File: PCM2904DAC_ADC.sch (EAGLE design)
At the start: 27 parts, among them Q1 12MHz, X1 V+, D-, D+, GND, X2 1503_09, X3 1503_09

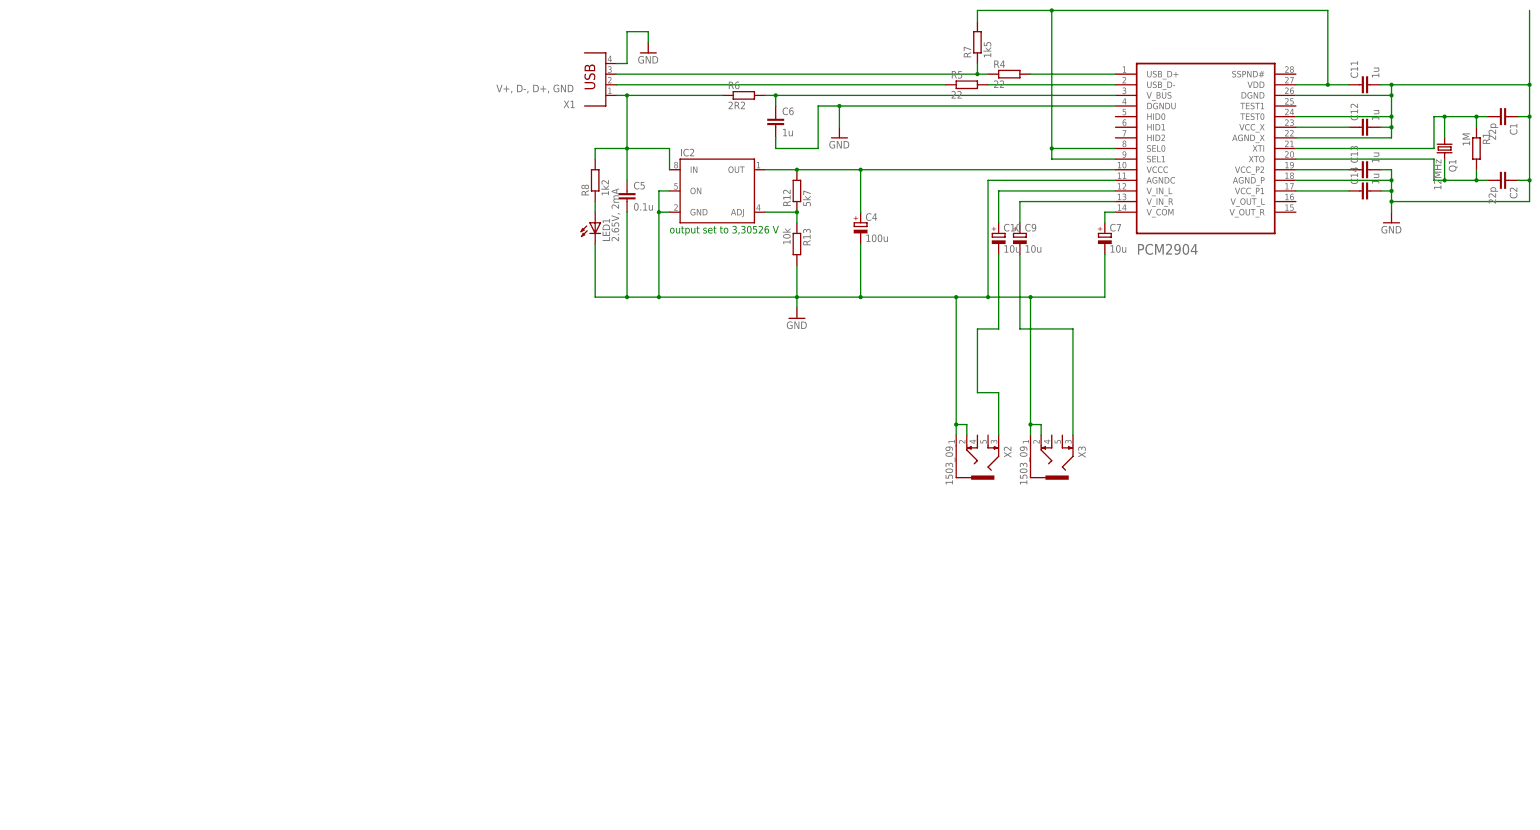
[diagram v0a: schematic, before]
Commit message: Agregados etapas preamplificadoras...
... y cambiado el ordenamiento y routeo de pistas
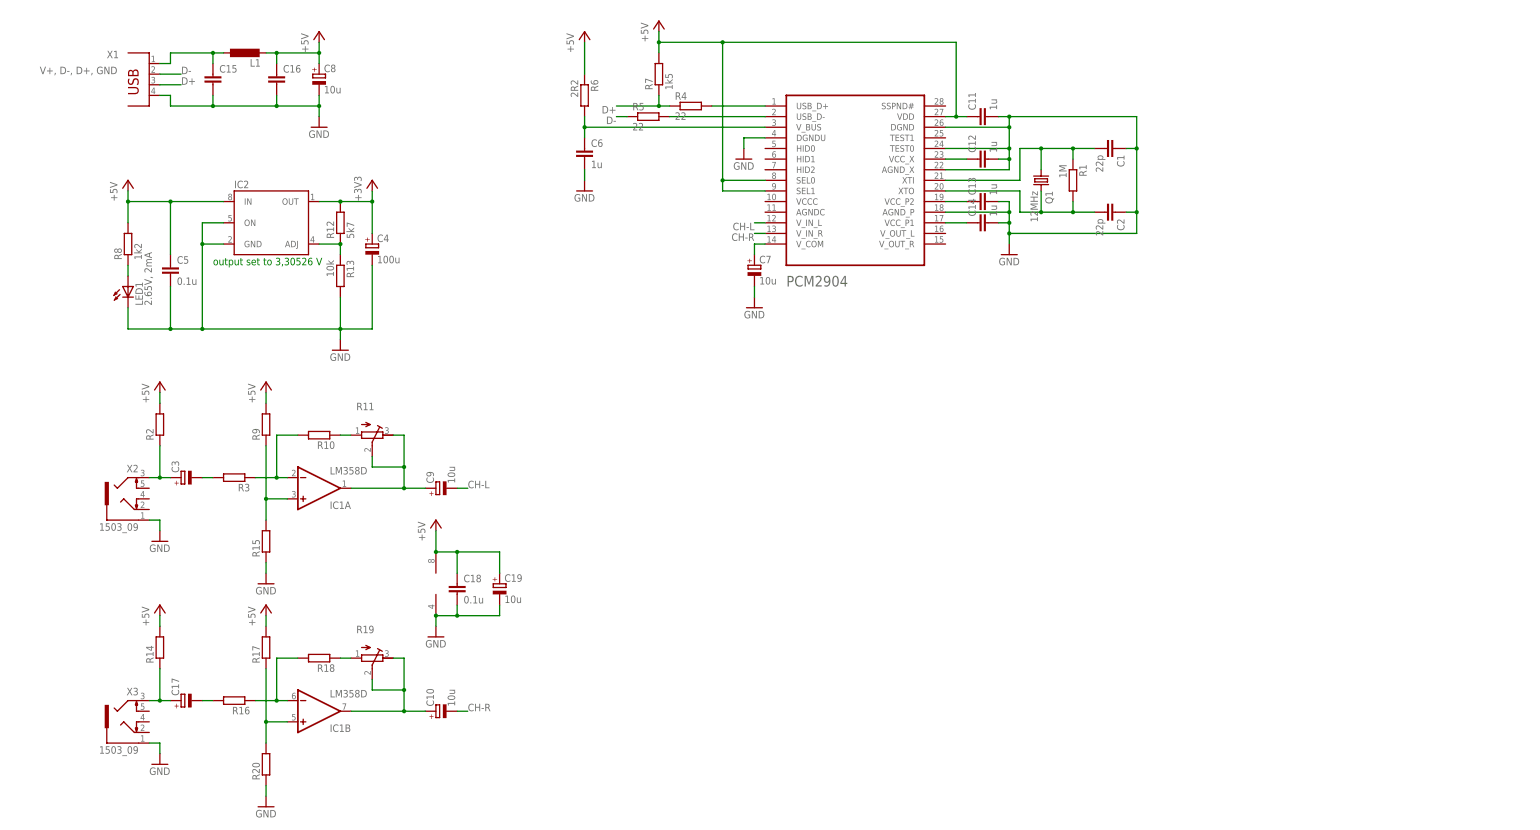
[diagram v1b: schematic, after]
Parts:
- added C15, C16: (no value), rcl:C-EUC1206K
- added C17, C3: (no value), rcl:CPOL-EU153CLV-0810
- added C18: 0.1u, rcl:C-EUC1206
- added C19, C8: 10u, rcl:CPOL-EUE2-4
- added IC1: LM358D, linear:LM358D
- added L1: (no value), rcl:L-EU0207/7
- added R10, R14, R15, R16, R17, R18, R2, R20, R3, R9: (no value), rcl:R-EU_R1206W
- added R11, R19: (no value), rcl:R-TRIMM64W
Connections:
- net N$7 renamed D+
- net N$8 renamed D-
- removed net N$40: C4.+, IC2.OUT, PCM2904.VCCC, R12.2
- new net +3V3: C4.+, IC2.OUT, R12.2
- new net +5V: C11.1, C16.1, C18.1, C19.+, C5.1, C8.+, IC1P.V+, IC2.IN, L1.2, PCM2904.SEL0, PCM2904.SEL1, PCM2904.VDD, R14.2, R17.2, R2.2, R6.1, R7.2, R8.2, R9.2
- new net CH-L: C9.-, PCM2904.V_IN_L
- new net CH-R: C10.-, PCM2904.V_IN_R
- new net N$17: R10.1, R11.A
- new net N$18: C9.+, IC1A.OUT, R11.E, R11.S
- new net N$19: IC1A.+IN, R15.2, R9.1
- new net N$22: IC1B.+IN, R17.1, R20.2
- new net N$5: C3.+, R2.1, X2.3
- new net N$7: C17.+, R14.1, X3.3
- new net N$8: C15.1, L1.1, X1.1
- net GND: now also C15.2, C16.2, C18.2, C19.-, C8.-, IC1P.V-, R15.1, R20.1; no longer PCM2904.AGNDC, X2.2, X3.2
- net N$10: now also IC1B.-IN, R16.1, R18.2; no longer C10.+, PCM2904.V_IN_L
- net N$12: now also R18.1, R19.A; no longer C11.1, PCM2904.SEL0, PCM2904.SEL1, PCM2904.VDD, R7.2
- net N$13: now also C3.-, R3.2; no longer C10.-, X2.3
- net N$14: now also C10.+, IC1B.OUT, R19.E, R19.S; no longer C9.+, PCM2904.V_IN_R
- net N$15: now also IC1A.-IN, R10.2, R3.1; no longer C9.-, X3.3
- net N$9: now also C17.-, R16.2; no longer C5.1, IC2.IN, R6.1, R8.2, X1.1
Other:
- moved on the sheet: C1, C10, C11, C12, C13, C14, C2, C4, C5, C6, C7, C9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

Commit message: Commit adicional
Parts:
- C10, C19, C8, C9: device rcl:CPOL-EUE2-4 -> rcl:CPOL-EU153CLV-0505
- C17, C3: device rcl:CPOL-EU153CLV-0810 -> rcl:CPOL-EU153CLV-0505
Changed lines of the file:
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@@
 <part name="GND4" library="supply1" deviceset="GND" device=""/>
 <part name="C7" library="rcl" deviceset="CPOL-EU" device="E2-4" value="10u"/>
-<part name="C9" library="rcl" deviceset="CPOL-EU" device="E2-4" value="10u"/>
+<part name="C9" library="rcl" deviceset="CPOL-EU" device="153CLV-0505" value="10u"/>
 <part name="GND1" library="supply1" deviceset="GND" device=""/>
 <part name="C11" library="rcl" deviceset="C-EU" device="C1206" value="1u"/>
@@
 <part name="R10" library="rcl" library_urn="urn:adsk.eagle:library:334" deviceset="R-EU_" device="R1206W" package3d_urn="urn:adsk.eagle:package:23539/1"/>
 <part name="R11" library="rcl" library_urn="urn:adsk.eagle:library:334" deviceset="R-TRIMM" device="64W" package3d_urn="urn:adsk.eagle:package:23748/1"/>
-<part name="C3" library="rcl" library_urn="urn:adsk.eagle:library:334" deviceset="CPOL-EU" device="153CLV-0810" package3d_urn="urn:adsk.eagle:package:23401/1"/>
+<part name="C3" library="rcl" deviceset="CPOL-EU" device="153CLV-0505" package3d_urn="urn:adsk.eagle:package:23402/1"/>
 <part name="R15" library="rcl" library_urn="urn:adsk.eagle:library:334" deviceset="R-EU_" device="R1206W" package3d_urn="urn:adsk.eagle:package:23539/1"/>
-<part name="C8" library="rcl" deviceset="CPOL-EU" device="E2-4" value="10u"/>
+<part name="C8" library="rcl" library_urn="urn:adsk.eagle:library:334" deviceset="CPOL-EU" device="153CLV-0505" package3d_urn="urn:adsk.eagle:package:23402/1" value="10u"/>
 <part name="C15" library="rcl" library_urn="urn:adsk.eagle:library:334" deviceset="C-EU" device="C1206K" package3d_urn="urn:adsk.eagle:package:23682/2"/>
 <part name="C16" library="rcl" library_urn="urn:adsk.eagle:library:334" deviceset="C-EU" device="C1206K" package3d_urn="urn:adsk.eagle:package:23682/2"/>
@@
 <part name="P+5" library="supply1" library_urn="urn:adsk.eagle:library:371" deviceset="+5V" device=""/>
 <part name="P+6" library="supply1" library_urn="urn:adsk.eagle:library:371" deviceset="+5V" device=""/>
-<part name="C10" library="rcl" deviceset="CPOL-EU" device="E2-4" value="10u"/>
+<part name="C10" library="rcl" library_urn="urn:adsk.eagle:library:334" deviceset="CPOL-EU" device="153CLV-0505" package3d_urn="urn:adsk.eagle:package:23402/1" value="10u"/>
 <part name="X3" library="con-lumberg" library_urn="urn:adsk.eagle:library:163" deviceset="1503_09" device="" package3d_urn="urn:adsk.eagle:package:8555/1"/>
 <part name="R14" library="rcl" library_urn="urn:adsk.eagle:library:334" deviceset="R-EU_" device="R1206W" package3d_urn="urn:adsk.eagle:package:23539/1"/>
@@
 <part name="R18" library="rcl" library_urn="urn:adsk.eagle:library:334" deviceset="R-EU_" device="R1206W" package3d_urn="urn:adsk.eagle:package:23539/1"/>
 <part name="R19" library="rcl" library_urn="urn:adsk.eagle:library:334" deviceset="R-TRIMM" device="64W" package3d_urn="urn:adsk.eagle:package:23748/1"/>
-<part name="C17" library="rcl" library_urn="urn:adsk.eagle:library:334" deviceset="CPOL-EU" device="153CLV-0810" package3d_urn="urn:adsk.eagle:package:23401/1"/>
+<part name="C17" library="rcl" deviceset="CPOL-EU" device="153CLV-0505" package3d_urn="urn:adsk.eagle:package:23402/1"/>
 <part name="R20" library="rcl" library_urn="urn:adsk.eagle:library:334" deviceset="R-EU_" device="R1206W" package3d_urn="urn:adsk.eagle:package:23539/1"/>
 <part name="P+7" library="supply1" library_urn="urn:adsk.eagle:library:371" deviceset="+5V" device=""/>
@@
 <part name="GND10" library="supply1" deviceset="GND" device=""/>
 <part name="C18" library="rcl" deviceset="C-EU" device="C1206" value="0.1u"/>
-<part name="C19" library="rcl" deviceset="CPOL-EU" device="E2-4" value="10u"/>
+<part name="C19" library="rcl" deviceset="CPOL-EU" device="153CLV-0505" value="10u"/>
 <part name="P+9" library="supply1" library_urn="urn:adsk.eagle:library:371" deviceset="+5V" device=""/>
 <part name="GND11" library="supply1" deviceset="GND" device=""/>

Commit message: Mas cosas
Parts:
- C4: device rcl:CPOL-EUE2-5 -> rcl:CPOL-EU153CLV-0505
- C7: device rcl:CPOL-EUE2-4 -> rcl:CPOL-EU153CLV-0505
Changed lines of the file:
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@@
 <part name="X1" library="con-berg" deviceset="PN61729" device="" value="V+, D-, D+, GND"/>
 <part name="GND2" library="supply1" deviceset="GND" device=""/>
-<part name="C4" library="rcl" deviceset="CPOL-EU" device="E2-5" value="100u "/>
+<part name="C4" library="rcl" deviceset="CPOL-EU" device="153CLV-0505" value="100u "/>
 <part name="R4" library="rcl" deviceset="R-EU_" device="R1206" value="22"/>
 <part name="R5" library="rcl" deviceset="R-EU_" device="R1206" value="22"/>
@@
 <part name="R7" library="rcl" deviceset="R-EU_" device="R1206" value="1k5"/>
 <part name="GND4" library="supply1" deviceset="GND" device=""/>
-<part name="C7" library="rcl" deviceset="CPOL-EU" device="E2-4" value="10u"/>
-<part name="C9" library="rcl" deviceset="CPOL-EU" device="153CLV-0505" value="10u"/>
+<part name="C7" library="rcl" library_urn="urn:adsk.eagle:library:334" deviceset="CPOL-EU" device="153CLV-0505" package3d_urn="urn:adsk.eagle:package:23402/1" value="10u"/>
+<part name="C9" library="rcl" deviceset="CPOL-EU" device="153CLV-0505" package3d_urn="urn:adsk.eagle:package:23402/1" value="10u"/>
 <part name="GND1" library="supply1" deviceset="GND" device=""/>
 <part name="C11" library="rcl" deviceset="C-EU" device="C1206" value="1u"/>
@@
 <part name="R10" library="rcl" library_urn="urn:adsk.eagle:library:334" deviceset="R-EU_" device="R1206W" package3d_urn="urn:adsk.eagle:package:23539/1"/>
 <part name="R11" library="rcl" library_urn="urn:adsk.eagle:library:334" deviceset="R-TRIMM" device="64W" package3d_urn="urn:adsk.eagle:package:23748/1"/>
-<part name="C3" library="rcl" deviceset="CPOL-EU" device="153CLV-0505" package3d_urn="urn:adsk.eagle:package:23402/1"/>
+<part name="C3" library="rcl" deviceset="CPOL-EU" device="153CLV-0505"/>
 <part name="R15" library="rcl" library_urn="urn:adsk.eagle:library:334" deviceset="R-EU_" device="R1206W" package3d_urn="urn:adsk.eagle:package:23539/1"/>
-<part name="C8" library="rcl" library_urn="urn:adsk.eagle:library:334" deviceset="CPOL-EU" device="153CLV-0505" package3d_urn="urn:adsk.eagle:package:23402/1" value="10u"/>
+<part name="C8" library="rcl" deviceset="CPOL-EU" device="153CLV-0505" package3d_urn="urn:adsk.eagle:package:23402/1" value="10u"/>
 <part name="C15" library="rcl" library_urn="urn:adsk.eagle:library:334" deviceset="C-EU" device="C1206K" package3d_urn="urn:adsk.eagle:package:23682/2"/>
 <part name="C16" library="rcl" library_urn="urn:adsk.eagle:library:334" deviceset="C-EU" device="C1206K" package3d_urn="urn:adsk.eagle:package:23682/2"/>
@@
 <part name="R18" library="rcl" library_urn="urn:adsk.eagle:library:334" deviceset="R-EU_" device="R1206W" package3d_urn="urn:adsk.eagle:package:23539/1"/>
 <part name="R19" library="rcl" library_urn="urn:adsk.eagle:library:334" deviceset="R-TRIMM" device="64W" package3d_urn="urn:adsk.eagle:package:23748/1"/>
-<part name="C17" library="rcl" deviceset="CPOL-EU" device="153CLV-0505" package3d_urn="urn:adsk.eagle:package:23402/1"/>
+<part name="C17" library="rcl" deviceset="CPOL-EU" device="153CLV-0505"/>
 <part name="R20" library="rcl" library_urn="urn:adsk.eagle:library:334" deviceset="R-EU_" device="R1206W" package3d_urn="urn:adsk.eagle:package:23539/1"/>
 <part name="P+7" library="supply1" library_urn="urn:adsk.eagle:library:371" deviceset="+5V" device=""/>
@@
 <part name="GND10" library="supply1" deviceset="GND" device=""/>
 <part name="C18" library="rcl" deviceset="C-EU" device="C1206" value="0.1u"/>
-<part name="C19" library="rcl" deviceset="CPOL-EU" device="153CLV-0505" value="10u"/>
+<part name="C19" library="rcl" library_urn="urn:adsk.eagle:library:334" deviceset="CPOL-EU" device="153CLV-0505" package3d_urn="urn:adsk.eagle:package:23402/1" value="10u"/>
 <part name="P+9" library="supply1" library_urn="urn:adsk.eagle:library:371" deviceset="+5V" device=""/>
 <part name="GND11" library="supply1" deviceset="GND" device=""/>
